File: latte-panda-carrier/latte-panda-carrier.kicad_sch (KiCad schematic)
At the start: 6 parts

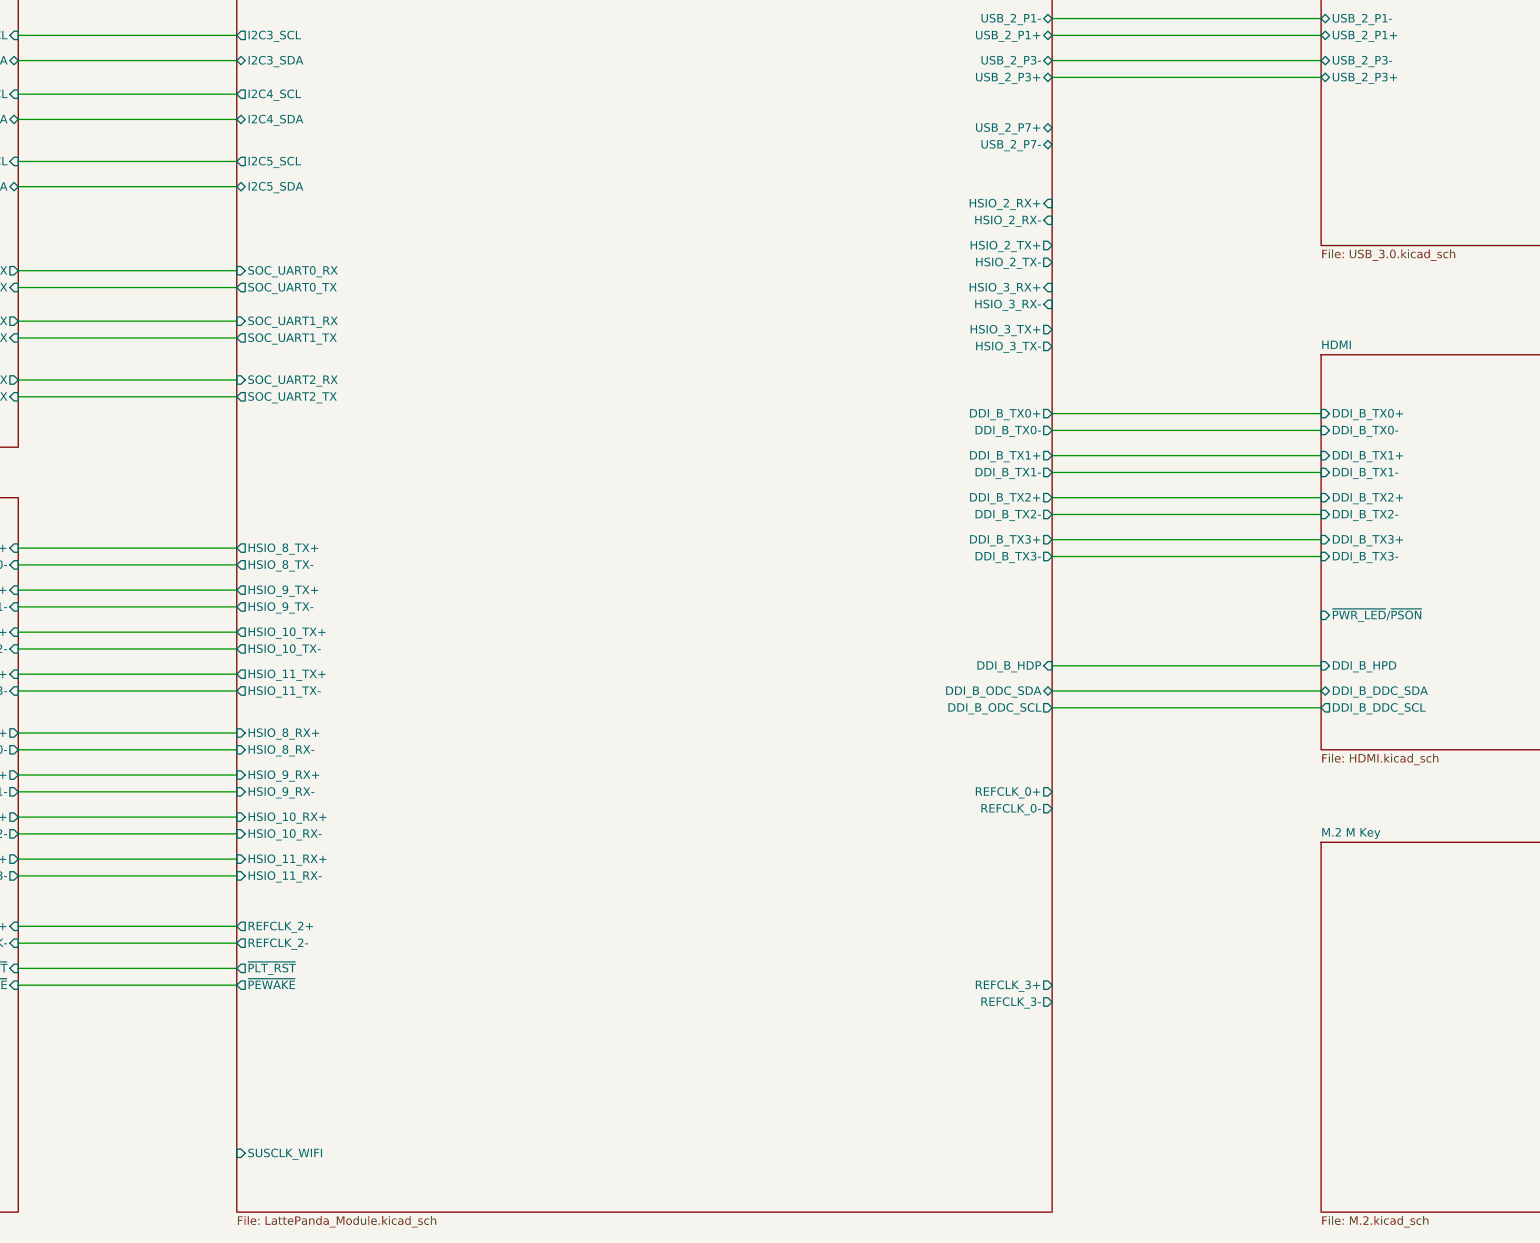
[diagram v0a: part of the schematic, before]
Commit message: Add m.2
Schematics stuff should be done, now.
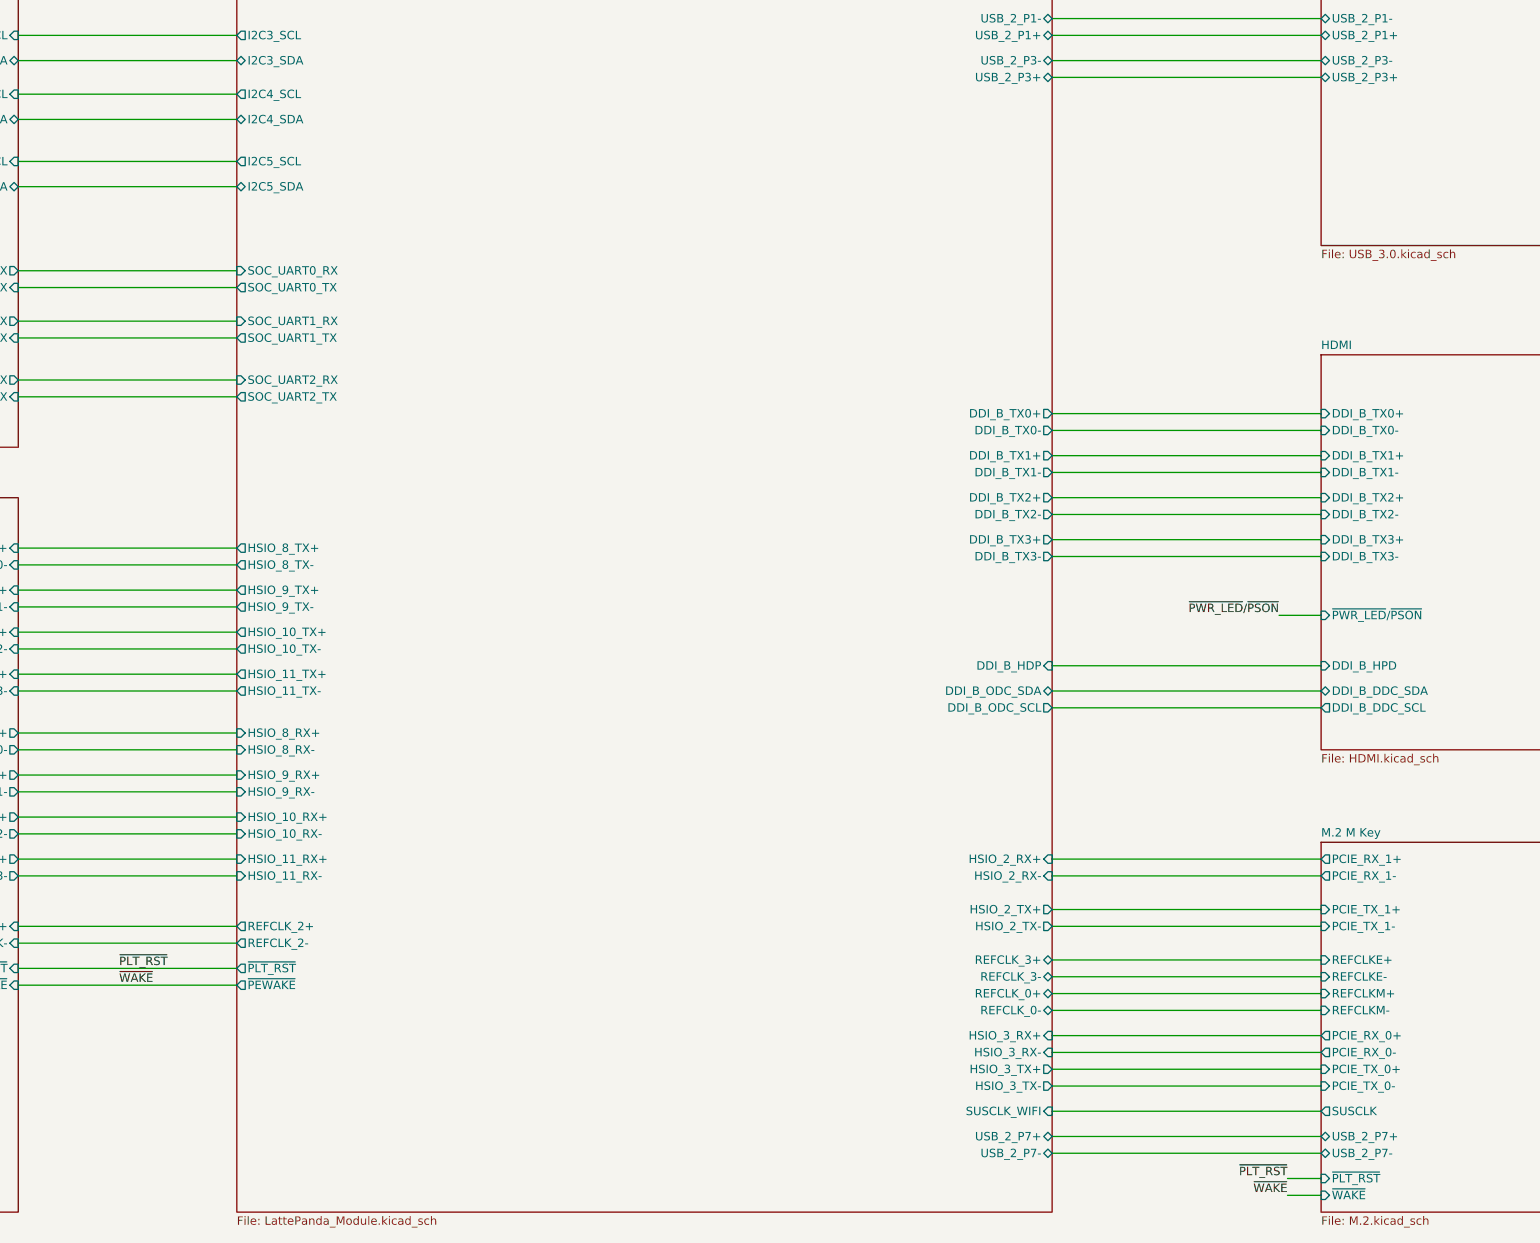
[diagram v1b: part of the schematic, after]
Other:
- sheet M.2 M Key ports: added PCIE_RX_0+, PCIE_RX_0-, PCIE_RX_1+, PCIE_RX_1-, PCIE_TX_0+, PCIE_TX_0-, PCIE_TX_1+, PCIE_TX_1-, REFCLKE+, REFCLKE-, REFCLKM+, REFCLKM-, SUSCLK, USB_2_P7+, USB_2_P7-, ~{PLT_RST}, ~{WAKE}; removed none
